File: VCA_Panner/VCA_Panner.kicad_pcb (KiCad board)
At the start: 2 copper layers, 43 x 110 mm, 81 parts, among them J1 CV1, J2 CV2, J3 Ch1_in, J4 Ch2_in, J5 Ch1_out, J6 Ch2_out, U1 AS3360, U2 TL074, U3 TL074, U4 TL074, U5 LM358

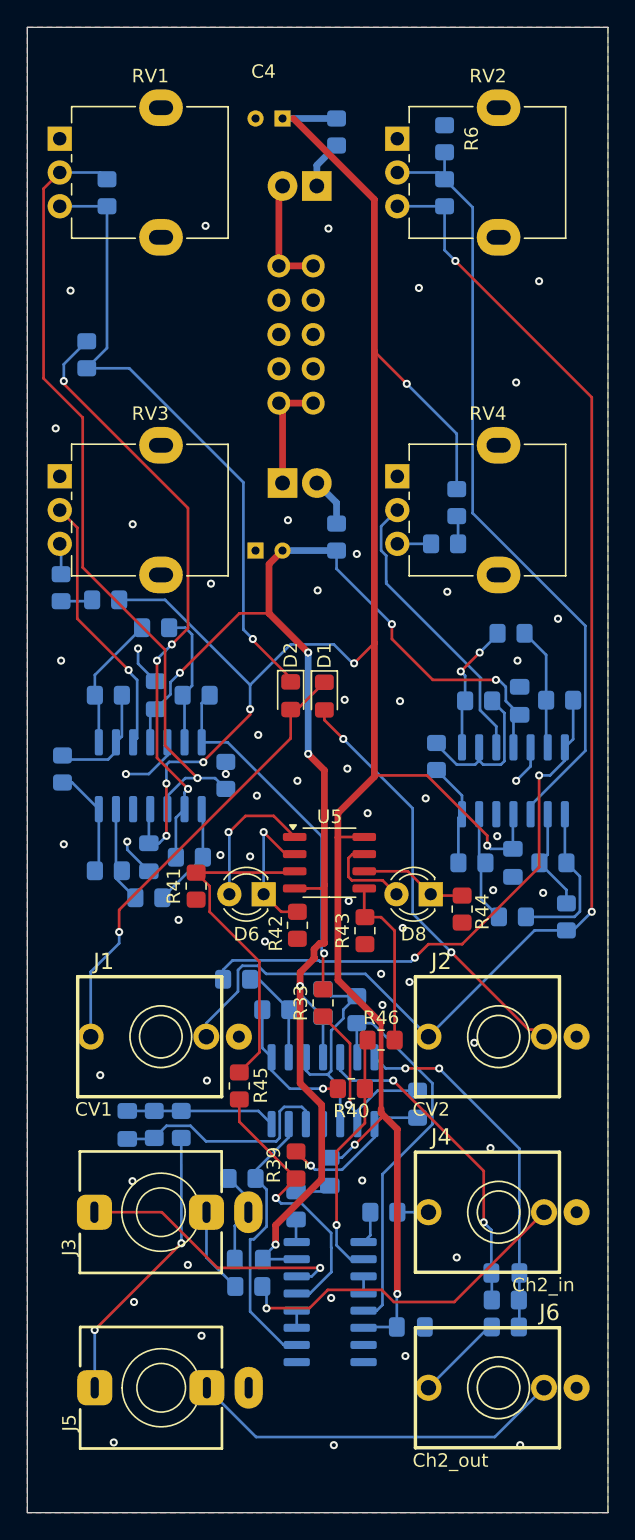
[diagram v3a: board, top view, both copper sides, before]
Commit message: vca panner fixes
fixed the footprint and audio routing. ditched the diodes for cv splitting.
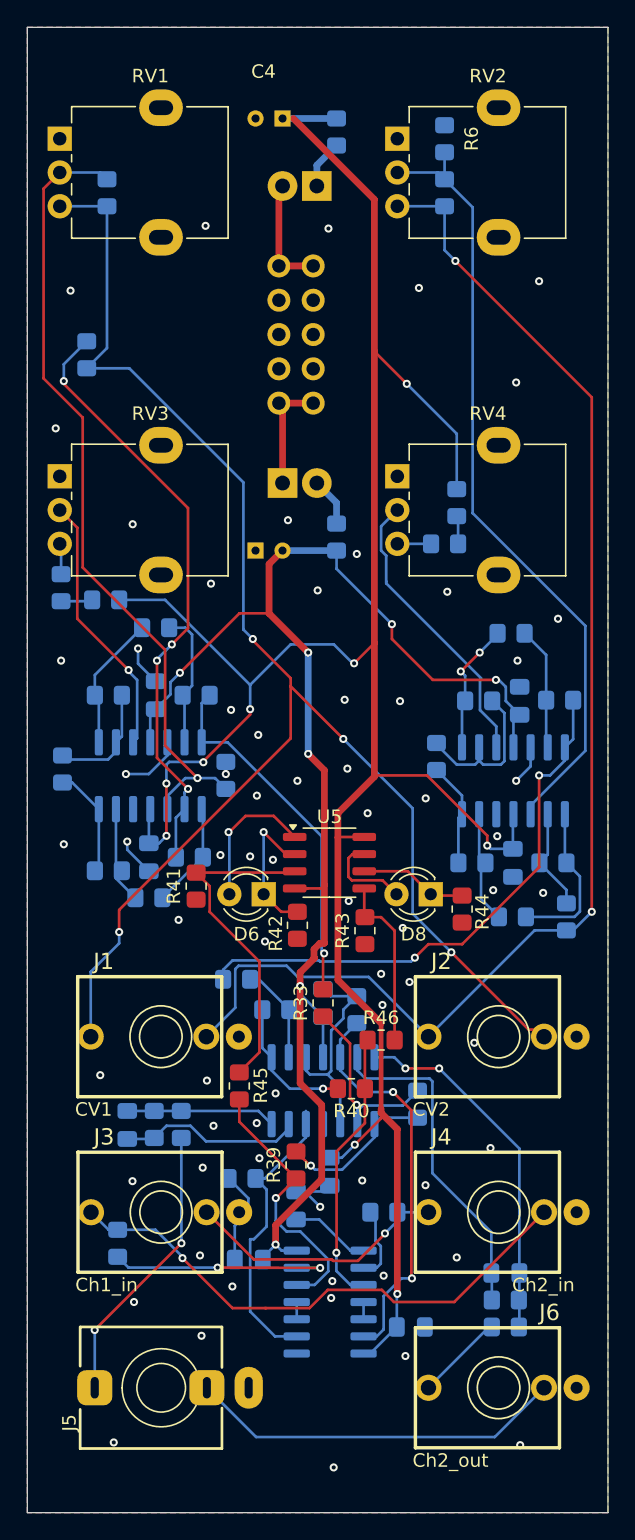
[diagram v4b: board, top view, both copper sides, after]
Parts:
- removed D1, D2: D, Diode_SMD:D_0805_2012Metric_Pad1.15x1.40mm_HandSolder
- removed R1: 51k, Resistor_SMD:R_0805_2012Metric_Pad1.20x1.40mm_HandSolder
- added R47: 51k, Resistor_SMD:R_0805_2012Metric_Pad1.20x1.40mm_HandSolder, B.Cu at (113.8, 147.3)
- J3: footprint mort_mix:Jack_3.5mm_QingPu_WQP-PJ366ST_Vertical -> mort_mix:PJ398SM
- U1: footprint Package_SO:SOIC-16_3.9x9.9mm_P1.27mm -> Package_SO:SO-14_3.9x8.65mm_P1.27mm
- turned J3 to 0 degrees
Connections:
- C2 pad 1: Net-(U2B-+) -> Net-(U2B--)
- C3 pad 1: Net-(U2D-+) -> Net-(U2D--)
- J1 pad T: Net-(D1-K) -> CV1
- J2 pad TN: Net-(D1-A) -> CV1
- J3 pad T: audio1_to_vca1 -> audio_to_ch2
- J4 pad T: Net-(J4-PadT) -> audio_to_ch1
- R13 pad 2: Net-(U2B-+) -> Net-(U2B--)
- R14 pad 2: Net-(U2D-+) -> Net-(U2D--)
- R2 pad 2: Net-(J4-PadT) -> audio_to_ch1
- U2 pad 12: Net-(U2D-+) -> Net-(U1B-IO2)
- U2 pad 13: Net-(U1B-IO2) -> Net-(U2D--)
- U2 pad 5: Net-(U2B-+) -> Net-(U1A-IO1)
- U2 pad 6: Net-(U1A-IO1) -> Net-(U2B--)
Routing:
- net CV1: track 47.5 -> 114.2 mm, vias 1 -> 4
- net Net-(D1-K): track 33.8 -> 0.00 mm, vias 1 -> 0
- net Net-(D1-A): track 31.3 -> 0.00 mm, vias 2 -> 0
- net Net-(U2D--): track 0.00 -> 24.9 mm
- net Net-(U2D-+): track 24.6 -> 0.00 mm, vias 2 -> 0
- net audio_to_ch1: track 0.00 -> 19.8 mm, vias 0 -> 1
- net Net-(U2B-+): track 17.4 -> 0.00 mm
- net audio_to_ch2: track 25.7 -> 40.9 mm
- net Net-(U2B--): track 0.00 -> 13.6 mm
- net Net-(J3-PadR): track 6.38 -> 0.00 mm
- net audio1_to_vca1: track 21.3 -> 17.0 mm, vias 1 -> 2
- net Net-(U1A-VREF): track 1.69 -> 5.96 mm
- net audio2_to_vca2: track 2.42 -> 5.54 mm
- net Net-(J4-PadT): track 2.31 -> 0.00 mm
- net GND: track 40.1 -> 42.4 mm, vias 57 -> 69
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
